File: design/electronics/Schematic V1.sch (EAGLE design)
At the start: 170 parts, among them J1 PJ-202AH, J2 PJ-025, J3 DD50P564GTXLF, J4 DD50P564GTXLF, J5 SAMTEC-TST-105-01-X-DJ, J6 SSW-106-02-TM-S-RA, SW1 TL6330AF200Q, U1 STM32F207VGT6TR, U10 SN65LBC175ADD16-M, U11 MAX7375AXR805+T21-0075D_MXM-M, U12 SN75ALS174ADWRDW20-M, U13 SN75468DRD0016A_M, U14 SN75468DRD0016A_M, U15 ACSL-6400-00TESOIC_6400-00TE-M, U16 ACSL-6400-00TESOIC_6400-00TE-M, U17 SN65LBC175ADD16-M, U18 SN65LBC175ADD16-M, U19 SN65LBC175ADD16-M, U2 LM2678S-5.0/NOPBTS7B-M, U21 RS0104YQTSSOP-14_JRT-M, U22 RS0104YQTSSOP-14_JRT-M, U24 RS0104YQTSSOP-14_JRT-M, U3 CDBC520-GCDBC-G-M, U4 TLV1117LV33DCYR, U5 LM43601PWPRPWP16_TEX-M, U6 RS0104YQTSSOP-14_JRT-M, U7 SN75ALS174ADWRDW20-M, U8 OPA4205APWRTSSOP14_PW_R-PDSO-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

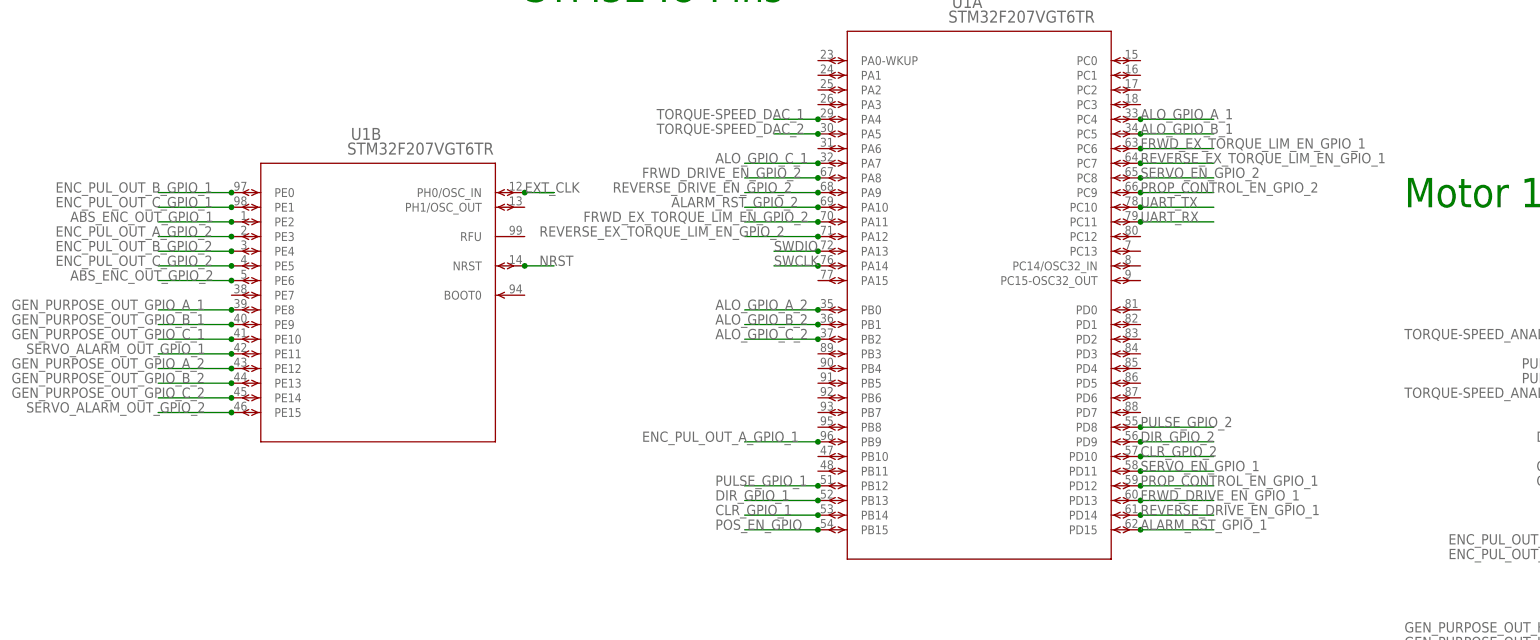
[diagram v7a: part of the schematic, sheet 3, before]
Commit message: Updated Layout with most ICs on board now
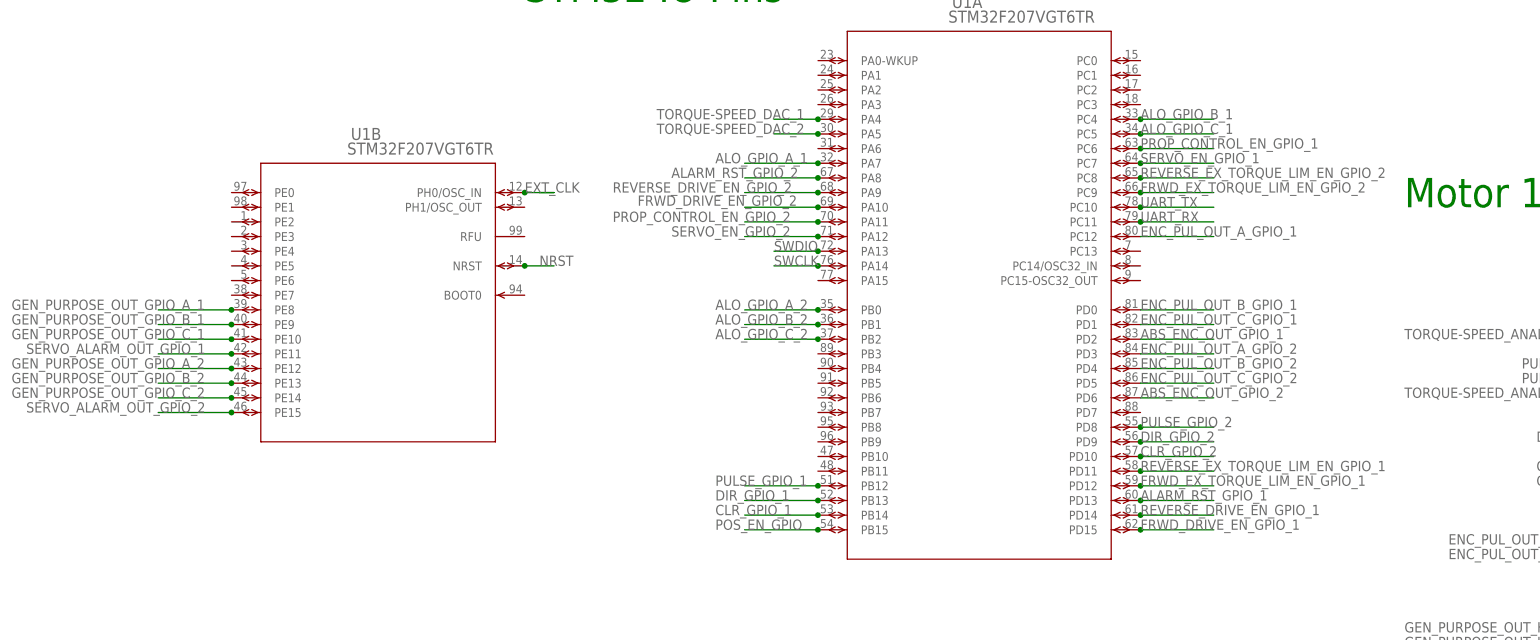
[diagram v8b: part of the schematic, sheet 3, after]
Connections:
- net ABS_ENC_OUT_GPIO_1: now also U1A.PD2; no longer U1B.PE2
- net ABS_ENC_OUT_GPIO_2: now also U1A.PD6; no longer U1B.PE6
- net ALARM_RST_GPIO_1: now also U1A.PD13; no longer U1A.PD15
- net ALARM_RST_GPIO_2: now also U1A.PA8; no longer U1A.PA10
- net ALO_GPIO_A_1: now also U1A.PA7; no longer U1A.PC4
- net ALO_GPIO_B_1: now also U1A.PC4; no longer U1A.PC5
- net ALO_GPIO_C_1: now also U1A.PC5; no longer U1A.PA7
- net ENC_PUL_OUT_A_GPIO_1: now also U1A.PC12; no longer U1A.PB9
- net ENC_PUL_OUT_A_GPIO_2: now also U1A.PD3; no longer U1B.PE3
- net ENC_PUL_OUT_B_GPIO_1: now also U1A.PD0; no longer U1B.PE0
- net ENC_PUL_OUT_B_GPIO_2: now also U1A.PD4; no longer U1B.PE4
- net ENC_PUL_OUT_C_GPIO_1: now also U1A.PD1; no longer U1B.PE1
- net ENC_PUL_OUT_C_GPIO_2: now also U1A.PD5; no longer U1B.PE5
- net FRWD_DRIVE_EN_GPIO_1: now also U1A.PD15; no longer U1A.PD13
- net FRWD_DRIVE_EN_GPIO_2: now also U1A.PA10; no longer U1A.PA8
- net FRWD_EX_TORQUE_LIM_EN_GPIO_1: now also U1A.PD12; no longer U1A.PC6
- net FRWD_EX_TORQUE_LIM_EN_GPIO_2: now also U1A.PC9; no longer U1A.PA11
- net PROP_CONTROL_EN_GPIO_1: now also U1A.PC6; no longer U1A.PD12
- net PROP_CONTROL_EN_GPIO_2: now also U1A.PA11; no longer U1A.PC9
- net REVERSE_EX_TORQUE_LIM_EN_GPIO_1: now also U1A.PD11; no longer U1A.PC7
- net REVERSE_EX_TORQUE_LIM_EN_GPIO_2: now also U1A.PC8; no longer U1A.PA12
- net SERVO_EN_GPIO_1: now also U1A.PC7; no longer U1A.PD11
- net SERVO_EN_GPIO_2: now also U1A.PA12; no longer U1A.PC8
